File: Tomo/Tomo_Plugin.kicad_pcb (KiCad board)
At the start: 2 copper layers, 35.6 x 55.9 mm, 20 parts, among them J002 STANDOFF_GND, J101 Raspberry_Pi_1, J102 CONN_01X02, J301 CONN_02X03, J401 CONN_01X04, J501 CONN_01X04, J601 CONN_01X04, U001 Designed_With_Kicad, U002 KwanSystems, U301 ADuM3221, U401 Arduino_Nano

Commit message: More changes
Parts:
- added REF**: Pin_Header_Straight_1x04_Pitch2.54mm, Pin_Headers:Pin_Header_Straight_1x04_Pitch2.54mm, F.Cu at (153.2, 130.4)
- added REF**: Pin_Header_Straight_1x03_Pitch2.54mm, Pin_Headers:Pin_Header_Straight_1x03_Pitch2.54mm, F.Cu at (160.8, 120.2)
- moved J102 37.5 mm to (127.8, 130.4), turned to 180 degrees
- moved R117 34.1 mm to (129.0, 129.1), turned to 90 degrees
- moved J501 28.6 mm to (160.8, 115.1), turned to 270 degrees
- moved D306 18.6 mm to (153.4, 147.6)
- moved R306 18.6 mm to (153.4, 148.9)
- moved J301 17.8 mm to (160.8, 150.7), turned to 270 degrees
- moved J401 7.62 mm to (127.8, 145.6), turned to 180 degrees
- moved U301 4.83 mm to (158.2, 144.3), turned to 180 degrees
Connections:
- J101 pad 1: Net-(J101-Pad1) -> (no net)
- J101 pad 13: Net-(J101-Pad13) -> (no net)
- J101 pad 16: Net-(J101-Pad16) -> (no net)
- J101 pad 18: Net-(J101-Pad18) -> (no net)
- J101 pad 19: Net-(J101-Pad19) -> (no net)
- J101 pad 21: Net-(J101-Pad21) -> (no net)
- J101 pad 22: Net-(J101-Pad22) -> (no net)
- J101 pad 23: Net-(J101-Pad23) -> (no net)
- J101 pad 24: Net-(J101-Pad24) -> (no net)
- J101 pad 26: Net-(J101-Pad26) -> (no net)
- J101 pad 7: Net-(J101-Pad7) -> (no net)
- J401 pad 2: /ENCODER0 -> /ENCODER1
- J401 pad 3: /ENCODER1 -> /ENCODER0
- J601 pad 5: Net-(J601-Pad5) -> (no net)
- U301 pad 2: /STEER -> /THROTTLE
- U301 pad 3: /THROTTLE -> /STEER
- U301 pad 6: /THROTTLE_HI -> /STEER_HI
- U301 pad 7: /STEER_HI -> /THROTTLE_HI
- U401 pad 16: Net-(U401-Pad16) -> (no net)
- U401 pad 17: Net-(U401-Pad17) -> (no net)
- U401 pad 18: Net-(U401-Pad18) -> (no net)
- U401 pad 19: Net-(U401-Pad19) -> (no net)
- U401 pad 20: Net-(U401-Pad20) -> (no net)
- U401 pad 21: Net-(U401-Pad21) -> (no net)
- U401 pad 22: Net-(U401-Pad22) -> (no net)
- U401 pad 28: Net-(U401-Pad28) -> (no net)
- U401 pad 30: Net-(U401-Pad30) -> (no net)
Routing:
- net +5V: track 35.3 -> 114.3 mm, vias 1 -> 2
- net /SDA: track 0.00 -> 64.9 mm, vias 0 -> 2
- net /SCL: track 0.00 -> 63.7 mm
- net +3V3: track 0.00 -> 58.1 mm
- net /GO_BTN: track 0.00 -> 35.7 mm, vias 0 -> 1
- net /E1_ECHO: track 0.00 -> 22.8 mm
- net /GPS_RX: track 0.00 -> 22.7 mm, vias 0 -> 1
- net /GPS_TX: track 0.00 -> 22.4 mm, vias 0 -> 1
- net /E0_ECHO: track 0.00 -> 21.2 mm
- net GND: track 0.00 -> 21.1 mm, vias 0 -> 2
- net /PPS: track 0.00 -> 18.2 mm
- net /THROTTLE: track 0.50 -> 15.7 mm
- net /STEER: track 0.50 -> 12.7 mm
- net +BATT: track 2.54 -> 11.7 mm
- net /STEER_HI: track 0.18 -> 7.83 mm, vias 0 -> 1
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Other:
- net class 5VPower added: clearance 0.1524, trace_width 0.254, via_dia 0.635, via_drill 0.3302
- board text added: "P"
- board text removed: "~FIX"

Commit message: Label changes
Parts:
- moved D417 2.29 mm to (130.6, 138.0), turned to 270 degrees
- moved D432 2.29 mm to (130.6, 145.6), turned to 90 degrees
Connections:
- J101 pad 1: (no net) -> Net-(J101-Pad1)
- J101 pad 13: (no net) -> Net-(J101-Pad13)
- J101 pad 16: (no net) -> Net-(J101-Pad16)
- J101 pad 18: (no net) -> Net-(J101-Pad18)
- J101 pad 19: (no net) -> Net-(J101-Pad19)
- J101 pad 21: (no net) -> Net-(J101-Pad21)
- J101 pad 22: (no net) -> Net-(J101-Pad22)
- J101 pad 23: (no net) -> Net-(J101-Pad23)
- J101 pad 24: (no net) -> Net-(J101-Pad24)
- J101 pad 26: (no net) -> Net-(J101-Pad26)
- J101 pad 7: (no net) -> Net-(J101-Pad7)
- J601 pad 5: (no net) -> Net-(J601-Pad5)
- U401 pad 16: (no net) -> Net-(U401-Pad16)
- U401 pad 17: (no net) -> Net-(U401-Pad17)
- U401 pad 18: (no net) -> Net-(U401-Pad18)
- U401 pad 19: (no net) -> Net-(U401-Pad19)
- U401 pad 20: (no net) -> Net-(U401-Pad20)
- U401 pad 21: (no net) -> Net-(U401-Pad21)
- U401 pad 22: (no net) -> Net-(U401-Pad22)
- U401 pad 28: (no net) -> Net-(U401-Pad28)
- U401 pad 30: (no net) -> Net-(U401-Pad30)
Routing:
- net GND: track 21.1 -> 1.95 mm, vias 2 -> 0
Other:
- board text added: "0 1"
- board text added: "3V3"
- board text added: "GND"
- board text added: "PWR"
- board text added: "SCL"
- board text added: "SDA"
- board text added: "Tomo Plugin 5.0"
- board text removed: "PW"
- board text removed: "Tomo 5.0"

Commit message: Removed KiCad_BOM_Wizard. As that was the file causing the nullsha1 problem, hopefully this fixes it
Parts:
- renumbered REF** to J502, REF** to J503
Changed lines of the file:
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@@
-(kicad_pcb (version 20170123) (host pcbnew "(2017-06-29 revision 413008344)-makepkg")
+(kicad_pcb (version 4) (host pcbnew 4.0.6-e0-6349~53~ubuntu16.04.1)
   (general
+    (links 68)
+    (no_connects 0)
+    (area 105.967599 85.707599 175.942401 157.197401)
     (thickness 1.6)
     (drawings 30)
@@
       (hpglpenspeed 20)
       (hpglpendiameter 15)
+      (hpglpenoverlay 2)
       (psnegative false)
       (psa4output false)
@@
     (descr "Through hole straight pin header, 1x04, 2.54mm pitch, single row")
     (tags "Through hole pin header THT 1x04 2.54mm single row")
-    (fp_text reference REF** (at 0 -2.33 90) (layer F.SilkS) hide
+    (fp_text reference J503 (at 0 -2.33 90) (layer F.SilkS) hide
       (effects (font (size 1 1) (thickness 0.15)))
     )
@@
     (descr "Through hole straight pin header, 1x03, 2.54mm pitch, single row")
     (tags "Through hole pin header THT 1x03 2.54mm single row")
-    (fp_text reference REF** (at 0 -2.33) (layer F.SilkS) hide
+    (fp_text reference J502 (at 0 -2.33) (layer F.SilkS) hide
       (effects (font (size 1 1) (thickness 0.15)))
     )
@@
     (fp_arc (start 13.97 36.83) (end 16.51 36.83) (angle 90) (layer F.Fab) (width 0.01))
     (fp_arc (start 13.97 -1.27) (end 13.97 -3.81) (angle 90) (layer F.Fab) (width 0.01))
-    (fp_text user TX1 (at 2.54 0) (layer F.SilkS)
+    (fp_text user TX1 (at 2.54 0 360) (layer F.SilkS)
       (effects (font (size 0.8128 0.8128) (thickness 0.1016)))
     )
@@
       (effects (font (size 1 1) (thickness 0.15)))
     )
-    (fp_text user RX0 (at 2.54 2.54) (layer F.SilkS)
+    (fp_text user RX0 (at 2.54 2.54 360) (layer F.SilkS)
       (effects (font (size 0.8128 0.8128) (thickness 0.1016)))
     )
@@
   (gr_line (start 127.77 154.5) (end 160.79 154.5) (angle 90) (layer Edge.Cuts) (width 0.15))
   (gr_line (start 126.5 99.89) (end 126.5 153.23) (angle 90) (layer Edge.Cuts) (width 0.15))
+  (segment (start 160.536 110.812) (end 160.282 111.066) (width 0.1524) (layer B.Cu) (net 0))
   (segment (start 161.2345 106.875) (end 161.2345 111.32) (width 0.254) (layer B.Cu) (net 1))
   (segment (start 159.52 121.48) (end 159.52 113.0345) (width 0.254) (layer B.Cu) (net 1))
@@
   (via (at 160.536 105.732) (size 0.635) (drill 0.3302) (layers F.Cu B.Cu) (net 1))
   (segment (start 129.04 101.16) (end 131.58 101.16) (width 1.6764) (layer F.Cu) (net 1))
-  (segment (start 160.536 110.812) (end 160.282 111.066) (width 0.1524) (layer B.Cu) (net 2))
   (segment (start 160.282 111.066) (end 160.282 109.834) (width 0.1524) (layer F.Cu) (net 2))
   (segment (start 160.282 109.834) (end 160.028 109.58) (width 0.1524) (layer F.Cu) (net 2))

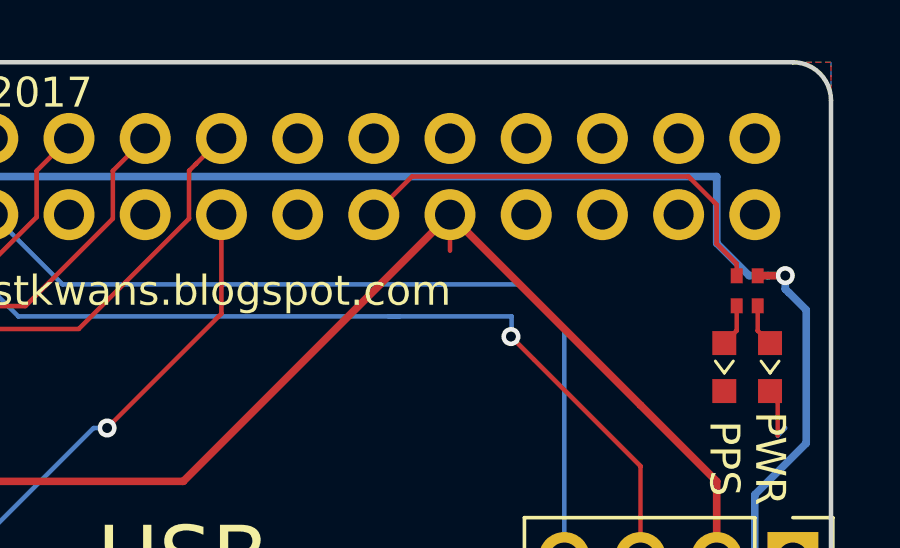
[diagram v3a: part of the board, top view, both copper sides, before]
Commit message: Redid encoder to use RP2 parts
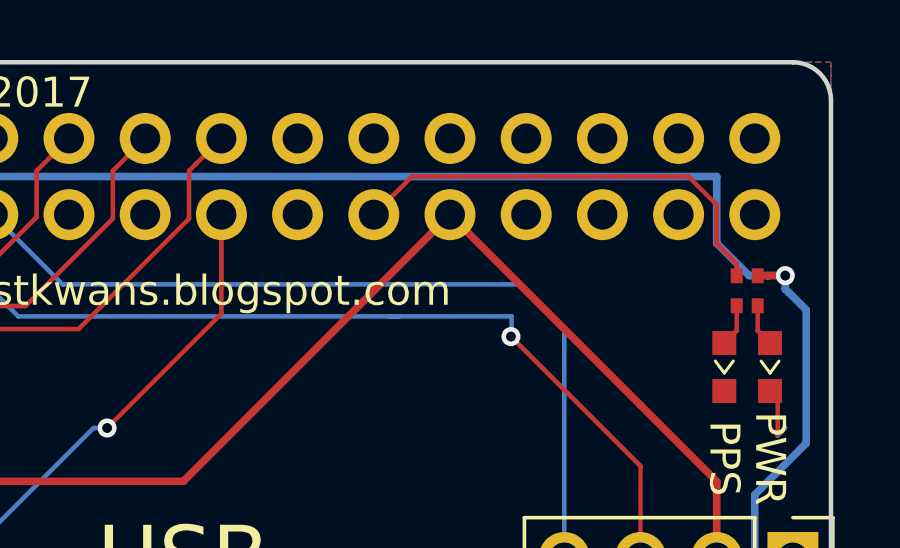
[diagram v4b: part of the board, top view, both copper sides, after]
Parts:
- J502: value Pin_Header_Straight_1x03_Pitch2.54mm -> CONN_01X03
- J503: value Pin_Header_Straight_1x04_Pitch2.54mm -> CONN_01X04
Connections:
- J101 pad 1: Net-(J101-Pad1) -> (no net)
- J101 pad 13: Net-(J101-Pad13) -> (no net)
- J101 pad 16: Net-(J101-Pad16) -> (no net)
- J101 pad 18: Net-(J101-Pad18) -> (no net)
- J101 pad 19: Net-(J101-Pad19) -> (no net)
- J101 pad 21: Net-(J101-Pad21) -> (no net)
- J101 pad 22: Net-(J101-Pad22) -> (no net)
- J101 pad 23: Net-(J101-Pad23) -> (no net)
- J101 pad 24: Net-(J101-Pad24) -> (no net)
- J101 pad 26: Net-(J101-Pad26) -> (no net)
- J101 pad 7: Net-(J101-Pad7) -> (no net)
- J601 pad 5: Net-(J601-Pad5) -> (no net)
- U401 pad 16: Net-(U401-Pad16) -> (no net)
- U401 pad 17: Net-(U401-Pad17) -> (no net)
- U401 pad 18: Net-(U401-Pad18) -> (no net)
- U401 pad 19: Net-(U401-Pad19) -> (no net)
- U401 pad 20: Net-(U401-Pad20) -> (no net)
- U401 pad 21: Net-(U401-Pad21) -> (no net)
- U401 pad 22: Net-(U401-Pad22) -> (no net)
- U401 pad 28: Net-(U401-Pad28) -> (no net)
- U401 pad 30: Net-(U401-Pad30) -> (no net)
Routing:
- net +3V3: track 58.1 -> 56.9 mm

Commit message: j
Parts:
- removed R413: 680, KwanSystems:R_Array_Convex_2x0402
- added U501: MPU9250, KwanSystems:Axis, F.Cu at (157.5, 136.0)
- R122: footprint KwanSystems:R_Array_Convex_2x0402 -> KwanSystems:R_Array_Convex_4x0402
- moved D432 36.8 mm to (136.9, 109.3)
- moved D417 29.1 mm to (135.4, 109.3), turned to 90 degrees
- moved D401 27.7 mm to (132.3, 109.3)
- moved D122 24.6 mm to (133.9, 109.3)
- moved R122 24.6 mm to (134.6, 106.2), turned to 90 degrees
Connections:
- R122 pad 1: +5V -> /PWRLED+
- R122 pad 2: /PPS_ECHO -> /PPS_ECHO+
- R122 pad 3: /PPS_ECHO+ -> /E1_ECHO+
- R122 pad 4: /PWRLED+ -> /E0_ECHO+
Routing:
- net +5V: track 114.3 -> 96.0 mm, vias 2 -> 3
- net /E1_ECHO+: track 7.74 -> 1.97 mm
- net /E0_ECHO+: track 7.73 -> 2.43 mm
- net /E0_ECHO: track 21.2 -> 25.6 mm, vias 0 -> 1
- net /SCL: track 63.7 -> 66.5 mm, vias 0 -> 2
- net /PPS: track 18.2 -> 20.3 mm
- net /SDA: track 64.9 -> 66.9 mm
- net GND: track 1.59 -> 0.00 mm
- net /GPS_RX: track 22.7 -> 24.0 mm
- net /PPS_ECHO: track 15.0 -> 13.7 mm, vias 0 -> 1
- net /E1_ECHO: track 22.8 -> 24.0 mm, vias 0 -> 1
- net /PWRLED+: track 1.41 -> 2.61 mm
- net /PPS_ECHO+: track 1.41 -> 1.97 mm
- net /GPS_TX: track 22.4 -> 22.2 mm, vias 1 -> 0
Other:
- board text added: "10 Jul 2017"
- board text added: "E0"
- board text added: "E1"
- board text removed: "10 May 2017"

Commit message: Files as ordered
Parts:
- removed D122: RED, KwanSystems:D_0603
- removed D401: GREEN, KwanSystems:D_0603
- added D115: RED, KwanSystems:D_0603, F.Cu at (146.8, 109.0)
- added R115: 1.5k, KwanSystems:SMD_0402, F.Cu at (146.8, 106.2)
- R122: value 680 -> RP2; footprint KwanSystems:R_Array_Convex_4x0402 -> KwanSystems:R_Array_Convex_2x0402
- moved R122 35.7 mm to (137.2, 141.8), turned to 0 degrees
- moved D417 34.1 mm to (130.6, 143.1), turned to 270 degrees
- moved D432 31.8 mm to (130.6, 140.5)
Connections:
- R122 pad 1: /PWRLED+ -> /E0_ECHO+
- R122 pad 2: /PPS_ECHO+ -> /E1_ECHO+
- R122 pad 3: /E1_ECHO+ -> /E1_ECHO
- R122 pad 4: /E0_ECHO+ -> /E0_ECHO
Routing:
- net /PPS_ECHO: track 13.7 -> 1.99 mm, vias 1 -> 0
- net GND: track 0.00 -> 7.93 mm, vias 0 -> 1
- net +5V: track 96.0 -> 90.0 mm
- net /E1_ECHO+: track 1.97 -> 7.21 mm
- net /E0_ECHO+: track 2.43 -> 7.21 mm
- net /E0_ECHO: track 25.6 -> 21.1 mm, vias 1 -> 2
- net +3V3: track 56.9 -> 59.7 mm
- net /PWRLED+: track 2.61 -> 0.00 mm
- net /SDA: track 66.9 -> 67.9 mm
- net /PPS_ECHO+: track 1.97 -> 1.44 mm
- net /E1_ECHO: vias 1 -> 2
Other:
- board text added: "Motor Power"
- board text added: "Tomo Plugin"
- board text added: "part of Project Yukari 5.0"
- board text removed: "0 1"
- board text removed: "E0"
- board text removed: "E1"
- board text removed: "PWR"
- board text removed: "Tomo Plugin 5.0"
- board text removed: "part of Project Yukari"

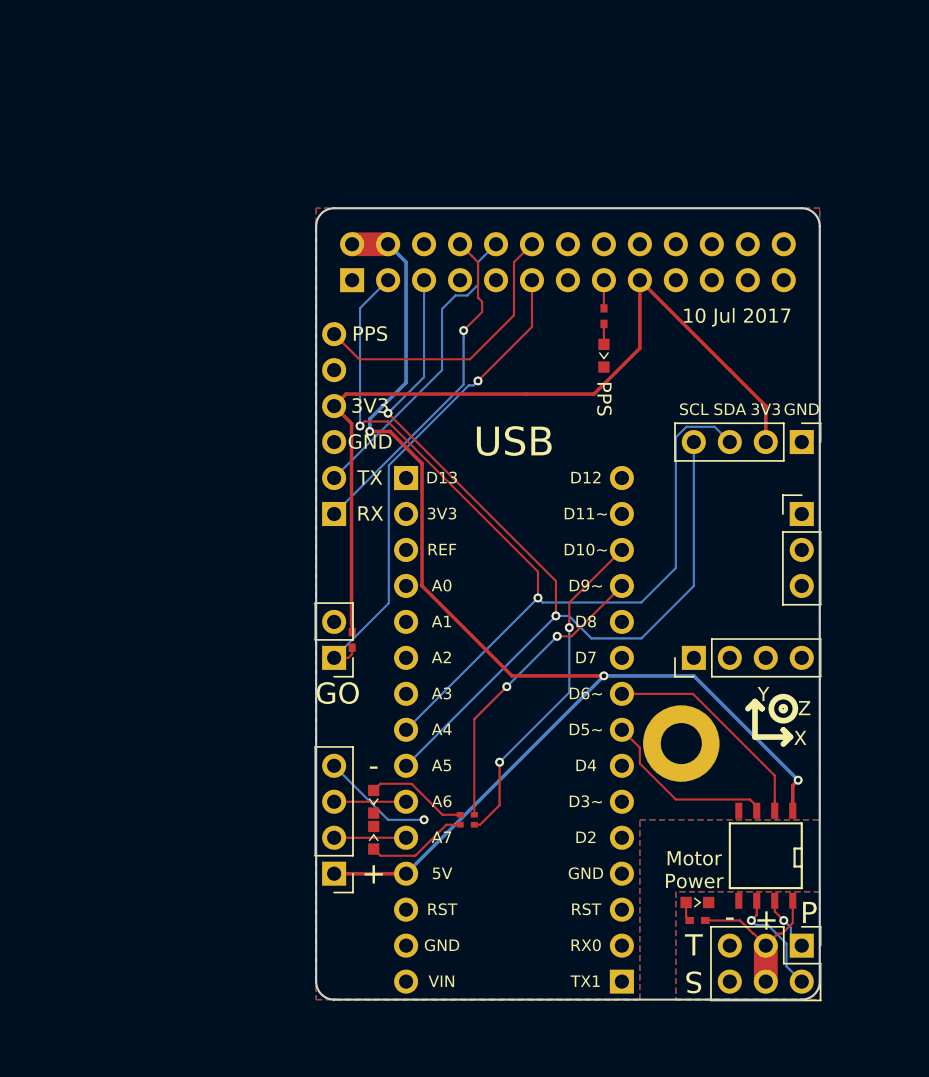
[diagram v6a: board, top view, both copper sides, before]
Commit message: Tomo soldermask fix, adding kwire stuff
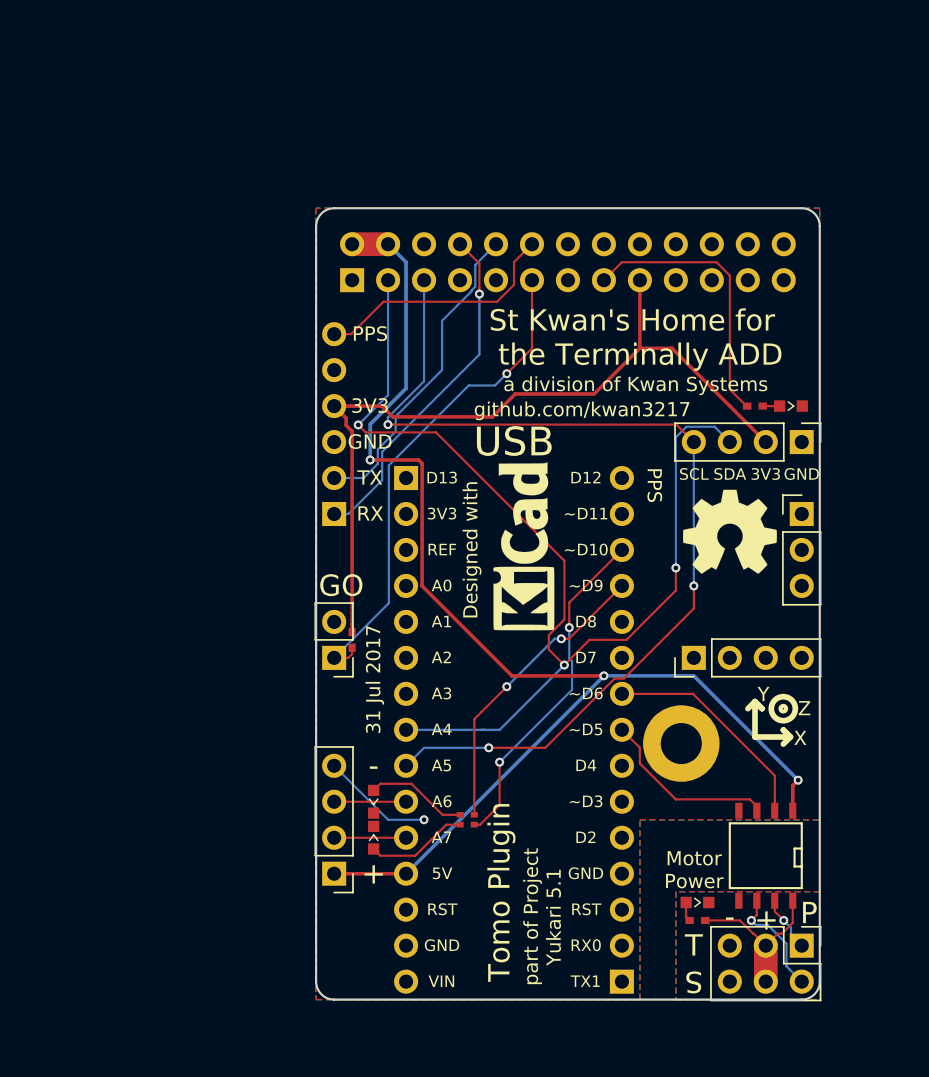
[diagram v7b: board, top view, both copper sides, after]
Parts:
- added G***: LOGO, KwanSystems:KWAN_CIRCLE, B.Cu at (140.5, 120.2)
- added REF**: KiCAD Logo, KwanSystems:Symbol_KiCAD-Logo_CopperAndSilkScreenTop_small, B.Cu at (144.3, 150.7)
- added REF***: OSHW-Symbol_6.7x6mm_SilkScreen, Symbols:OSHW-Symbol_6.7x6mm_SilkScreen, F.Cu at (155.7, 121.5)
- added REF***: OSHW-Symbol_6.7x6mm_Copper, KwanSystems:OSHW-Symbol_6.7x6mm_SolderMask, B.Cu at (137.9, 150.7)
- U001, U002: moved to F.Cu
- moved U001 29.2 mm to (141.0, 122.5), turned to 90 degrees
- moved U002 22.1 mm to (135.4, 109.3), turned to 0 degrees
- moved D115 13.7 mm to (160.0, 112.6), turned to 180 degrees
- moved R115 12.4 mm to (157.5, 112.6), turned to 0 degrees
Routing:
- net /PPS_ECHO: track 1.99 -> 19.6 mm
- net /SDA: track 67.9 -> 76.6 mm, vias 2 -> 3
- net /SCL: track 66.7 -> 70.1 mm, vias 2 -> 3
- net +3V3: track 59.7 -> 56.8 mm
- net /PPS: track 20.3 -> 17.5 mm
- net +5V: track 90.0 -> 91.2 mm
- net /GO_BTN: track 35.6 -> 36.5 mm
- net /GPS_TX: track 21.7 -> 22.5 mm
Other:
- rule pad_to_mask_clearance: 0.2 -> 0
- board text added: "31 Jul 2017"
- board text added: "github.com/kwan3217"
- board text added: "https://github.com/kwan3217"
- board text added: "https://stkwans.blogspot.com"
- board text added: "part of Project Yukari 5.1"
- board text removed: "10 Jul 2017"
- board text removed: "part of Project Yukari 5.0"
- board text removed: "stkwans.blogspot.com"
